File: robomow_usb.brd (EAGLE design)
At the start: 42 x 17.8 mm, 25 parts, among them IC1 FT231XS-R, J1 RJ11-2L-B, U1 SN65HVD1176

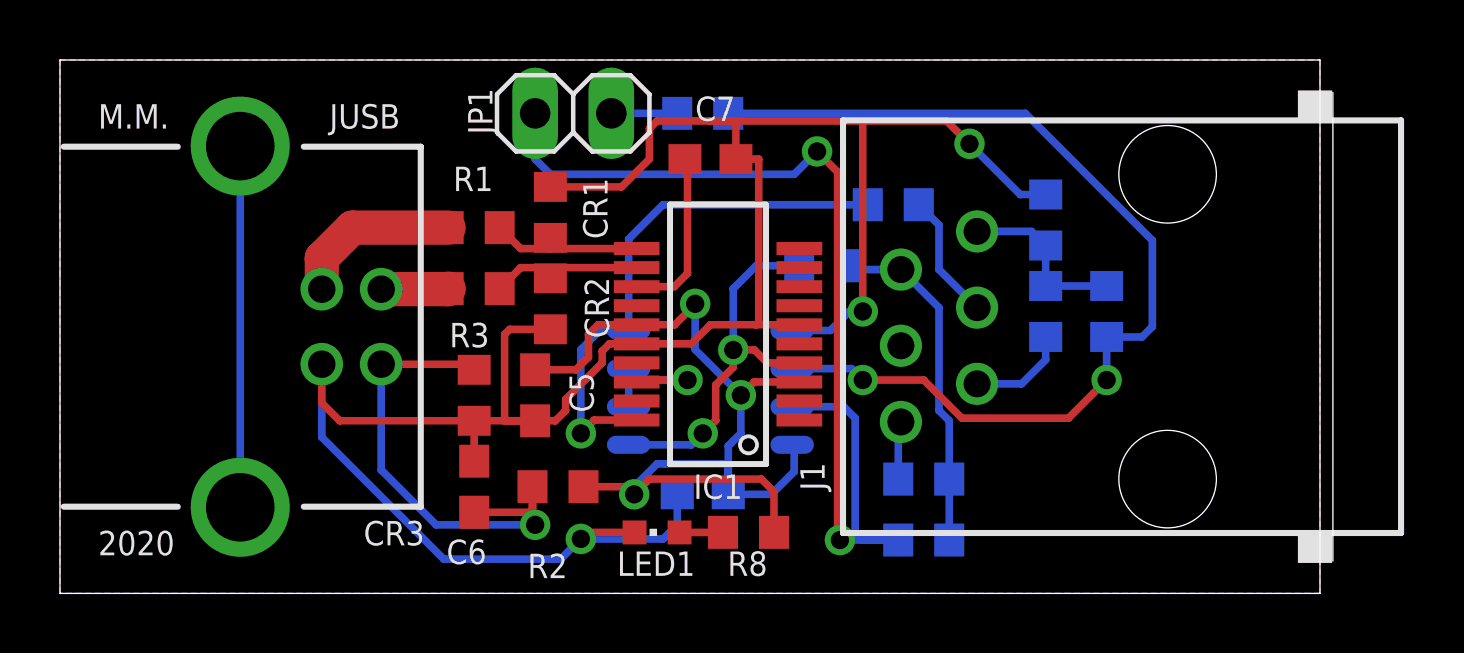
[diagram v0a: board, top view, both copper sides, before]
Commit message: Added TX RX LEDs
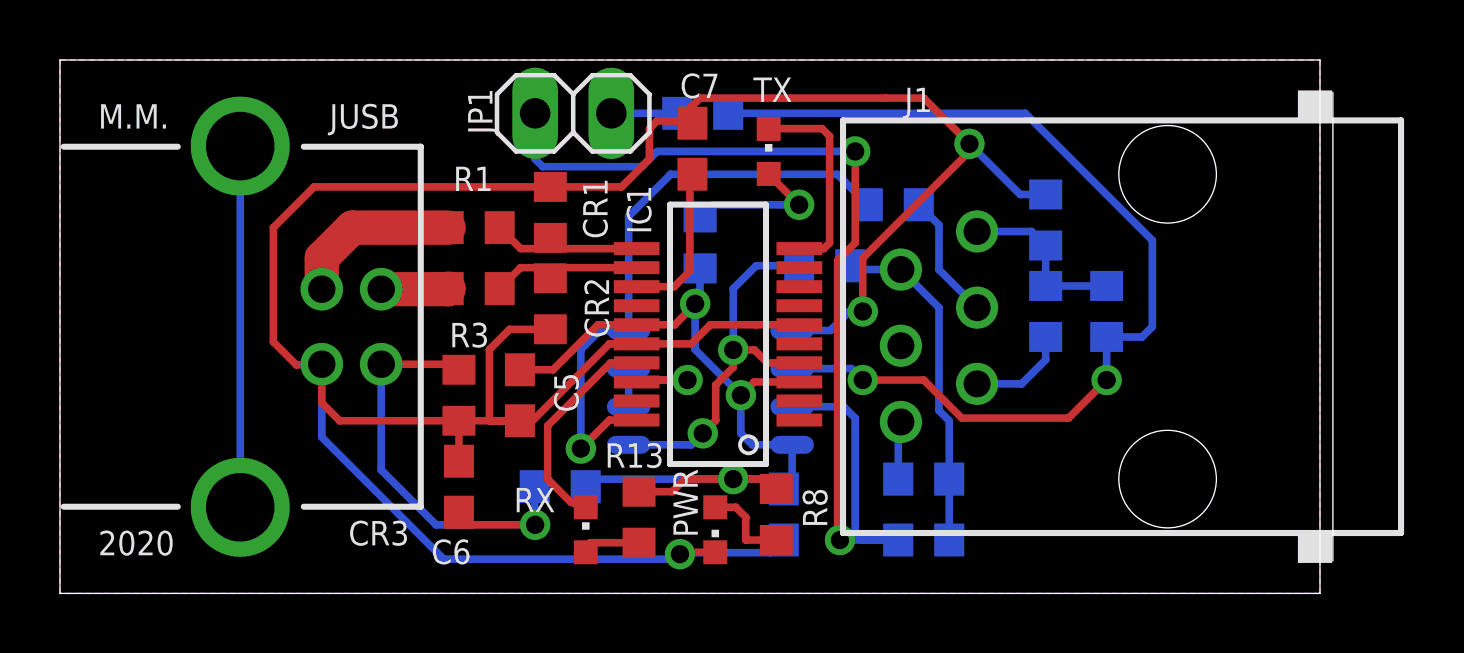
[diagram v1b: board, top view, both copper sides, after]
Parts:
- removed LED1: (no value), dp_devices:LED-603
- added PWR, RX, TX: (no value), dp_devices:LED-603
- added R13, R14: 470, rcl:R0603
- moved C1 2.79 mm to (24.1, 2.63), turned to 270 degrees
- moved R8 1.10 mm to (23.9, 2.63), turned to 270 degrees
- moved C7 0.69 mm to (21.1, 14.8), turned to 90 degrees
- moved C5 0.51 mm to (15.3, 6.60)
- moved C6 0.51 mm to (13.3, 3.56)
- moved CR3 0.51 mm to (13.3, 6.60)
- moved R2 0.07 mm to (16.7, 3.56), flipped to the bottom, turned to 180 degrees
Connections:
- new net VIN_LED_R2: R13.2, RX.A
- new net VIN_LED_R3: R14.2, TX.A
- net !RXLED: now also RX.C
- net !TXLED: now also TX.C
- net GND: now also PWR.C; no longer LED1.C
- net VCC_USB: now also R13.1, R14.1
- net VIN_LED_R1: now also PWR.A; no longer LED1.A
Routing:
- net GND: track 82.6 -> 93.0 mm
- net !RXLED: track 0.00 -> 7.23 mm
- net !TXLED: track 0.00 -> 6.78 mm
- net VIN_LED_R3: track 0.00 -> 4.92 mm, vias 0 -> 1
- net FTDI_TX: track 18.2 -> 20.2 mm
- net VIN_LED_R2: track 0.00 -> 1.98 mm
- net VCC_USB: track 32.3 -> 30.5 mm
- net VIN_LED_R1: track 1.45 -> 2.93 mm
- net RS485_B: track 34.1 -> 35.1 mm
- net VUSB: track 16.6 -> 16.1 mm

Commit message: Full pass on DRC (removed stubs)
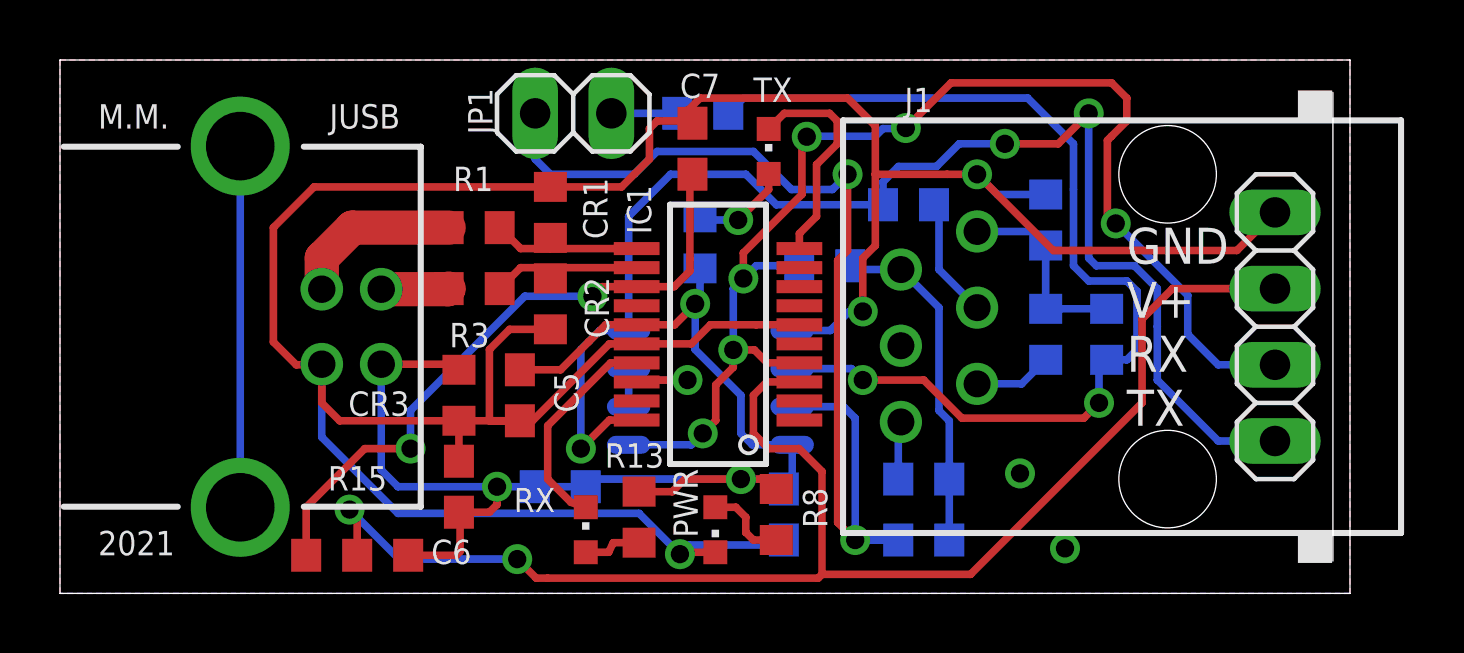
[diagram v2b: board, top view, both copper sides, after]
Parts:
- added JP2: (no value), pinhead:1X04
- added R15: R_POPOP0603, martonmiklos:0603_POPOP
- moved R10 0.76 mm to (32.9, 8.64)
- moved R11 0.76 mm to (34.9, 8.64)
- moved R7 0.51 mm to (28.3, 13.0)
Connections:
- removed net VCC_USB: C1.1, C5.1, IC1.15, IC1.3, R13.1, R14.1, R2.2, R8.1, U1.8
- new net VCC_IO: IC1.3, JP2.3, R15.COM
- net 3.3V: now also R15.A
- net FTDI_RX: now also JP2.2
- net FTDI_TX: now also JP2.1
- net GND: now also JP2.4
- net VUSB: now also C1.1, C5.1, IC1.15, R13.1, R14.1, R15.A1, R2.2, R8.1, U1.8
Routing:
- net VCC_IO: track 0.00 -> 48.3 mm, vias 0 -> 2
- net VUSB: track 16.1 -> 46.5 mm, vias 1 -> 3
- net VCC_USB: track 30.5 -> 0.00 mm, vias 3 -> 0
- net FTDI_RX: track 12.8 -> 42.6 mm, vias 2 -> 6
- net FTDI_TX: track 20.2 -> 44.6 mm, vias 1 -> 3
- net 3.3V: track 5.88 -> 22.1 mm, vias 0 -> 2
- net GND: track 93.0 -> 102.9 mm, vias 3 -> 5
- net VIN_LED_R3: track 4.92 -> 3.26 mm
- net RS485_A: track 33.6 -> 34.7 mm
- net RJ11_2: track 3.38 -> 2.62 mm
- net RJ11_6: track 5.86 -> 6.62 mm
- net !TXLED: track 6.78 -> 7.38 mm
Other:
- board size 42 x 17.8 mm -> 43 x 17.8 mm
- board text added: "2021"
- board text added: "GND V+ RX TX"
- board text removed: "2020"

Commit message: Fixup input filtering
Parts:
- J1: value RJ11-2L-B -> RJ11NO_DIMENSION; device con-tycoelectronics:RJ11-NO_SHIELD -> con-tycoelectronics:RJ11-NO_SHIELD_NO_DIMENSION
- PWR, RX, TX: value (none) -> LED_0603
- moved R2 4.95 mm to (13.8, 7.59), flipped to the top, turned to 0 degrees
- moved C6 2.06 mm to (13.0, 5.59), flipped to the bottom, turned to 270 degrees
- moved C5 1.57 mm to (14.9, 5.08)
- moved CR3 1.57 mm to (12.9, 5.08)
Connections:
- new net VUSB_CONN: C6.1, CR3.2, JUSB.VBUS, R2.1
- net VUSB: no longer C6.1, CR3.2, JUSB.VBUS, R2.1
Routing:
- net VUSB: track 46.5 -> 37.7 mm
- net VUSB_CONN: track 0.00 -> 8.31 mm
- net 3.3V: track 22.1 -> 23.9 mm
- net FTDI_TX: track 44.6 -> 44.1 mm
